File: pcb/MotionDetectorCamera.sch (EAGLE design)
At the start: 79 parts, among them J1 SOLDER-JUMPER, U1 ICE40HX4K-BG121, U2 TPS6280XYKAR, U3 TPS6280XYKAR, U4 W989D6DBGX6I, U5 TPS63805YFFR, U6 GD25LQ80CEIGR, X1 SIT8021AI-J4-18S-12.000000E

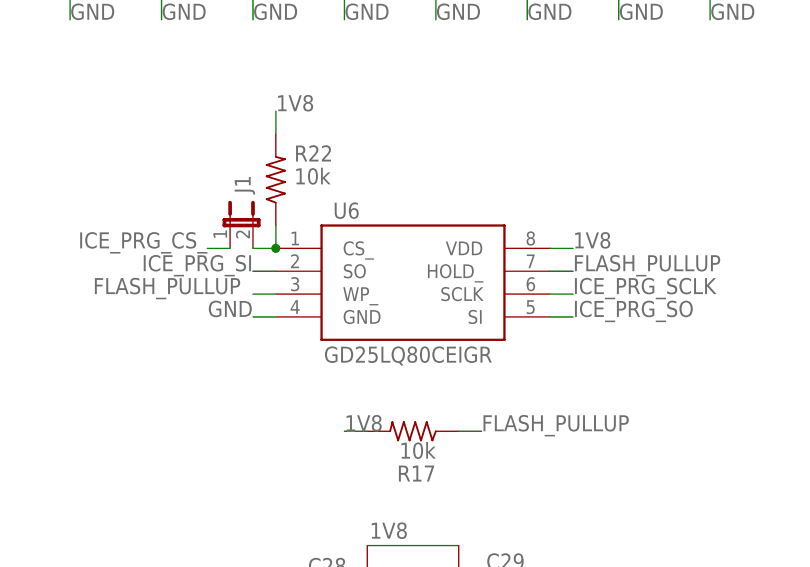
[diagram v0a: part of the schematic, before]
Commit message: Switch to W25Q80EWUXIE
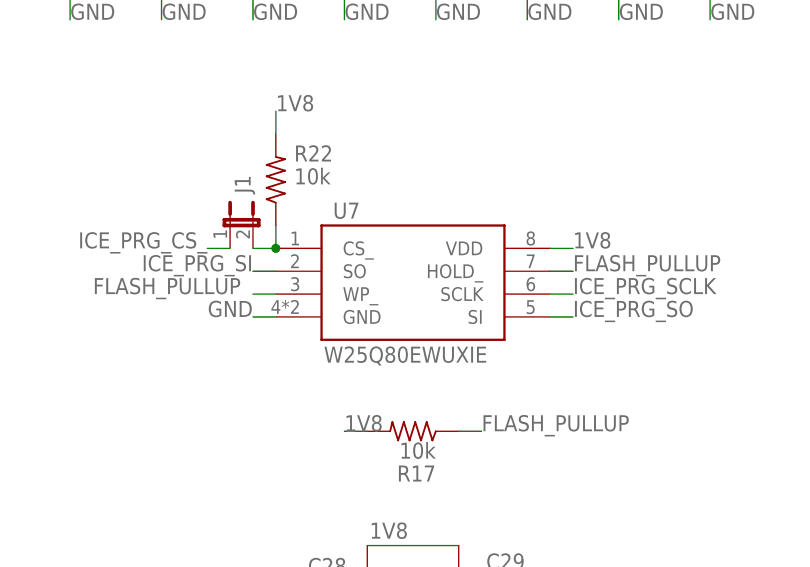
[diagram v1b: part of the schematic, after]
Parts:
- removed U6: GD25LQ80CEIGR, EagleLibrary:GD25LQ80CEIGR
- added U7: W25Q80EWUXIE, EagleLibrary:W25Q80EWUXIE
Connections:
- net 1V8: now also U7.VDD; no longer U6.VDD
- net FLASH_PULLUP: now also U7.HOLD_, U7.WP_; no longer U6.HOLD_, U6.WP_
- net GND: now also U7.GND; no longer U6.GND
- net ICE_PRG_SCLK: now also U7.SCLK; no longer U6.SCLK
- net ICE_PRG_SI: now also U7.SO; no longer U6.SO
- net ICE_PRG_SO: now also U7.SI; no longer U6.SI
- net N$3: now also U7.CS_; no longer U6.CS_
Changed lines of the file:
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@@
 <attribute name="PN" value="GRM155R61H104KE19D"/>
 </part>
-<part name="U6" library="EagleLibrary" deviceset="GD25LQ80CEIGR" device="" package3d_urn="urn:adsk.eagle:package:17077898/1"/>
 <part name="R17" library="EagleLibrary" deviceset="RESISTOR" device="0402" package3d_urn="urn:adsk.eagle:package:17080064/1" value="10k">
 <attribute name="MFG" value="Vishay"/>
@@
 </part>
 <part name="J1" library="EagleLibrary" deviceset="SOLDER-JUMPER" device=""/>
+<part name="U7" library="EagleLibrary" deviceset="W25Q80EWUXIE" device="" package3d_urn="urn:adsk.eagle:package:18792578/1"/>
 </parts>
 <sheets>
@@
 <attribute name="MFG" x="83.82" y="68.58" size="1.778" layer="96" display="off"/>
 </instance>
-<instance part="U6" gate="G$1" x="378.46" y="121.92" smashed="yes">
-<attribute name="NAME" x="369.57" y="127.762" size="1.778" layer="95"/>
-<attribute name="PN" x="368.554" y="111.76" size="1.778" layer="95"/>
-</instance>
 <instance part="R17" gate="G$1" x="378.46" y="104.14" smashed="yes" rot="R180">
 <attribute name="NAME" x="381" y="100.33" size="1.778" layer="95" rot="R180"/>
@@
 <instance part="J1" gate="G$1" x="360.68" y="127" smashed="yes">
 <attribute name="NAME" x="358.648" y="130.556" size="1.778" layer="95" rot="R90" align="top-left"/>
+</instance>
+<instance part="U7" gate="G$1" x="368.3" y="127" smashed="yes">
+<attribute name="NAME" x="369.57" y="127.762" size="1.778" layer="95"/>
+<attribute name="PN" x="368.554" y="111.76" size="1.778" layer="95"/>
 </instance>
 </instances>
@@
 </segment>
 <segment>
-<pinref part="U6" gate="G$1" pin="VDD"/>
 <wire x1="393.7" y1="124.46" x2="396.24" y2="124.46" width="0.1524" layer="91"/>
 <label x="396.24" y="124.46" size="1.778" layer="95"/>
+<pinref part="U7" gate="G$1" pin="VDD"/>
 </segment>
 <segment>
@@
 </segment>
 <segment>
-<pinref part="U6" gate="G$1" pin="GND"/>
 <wire x1="363.22" y1="116.84" x2="360.68" y2="116.84" width="0.1524" layer="91"/>
 <label x="360.68" y="116.84" size="1.778" layer="95" align="bottom-right"/>
+<pinref part="U7" gate="G$1" pin="GND"/>
 </segment>
 <segment>
@@
 </segment>
 <segment>
-<pinref part="U6" gate="G$1" pin="SI"/>
 <wire x1="393.7" y1="116.84" x2="396.24" y2="116.84" width="0.1524" layer="91"/>
 <label x="396.24" y="116.84" size="1.778" layer="95"/>
+<pinref part="U7" gate="G$1" pin="SI"/>
 </segment>
 </net>
@@
 </segment>
 <segment>
-<pinref part="U6" gate="G$1" pin="SO"/>
 <wire x1="363.22" y1="121.92" x2="360.68" y2="121.92" width="0.1524" layer="91"/>
 <label x="360.68" y="121.92" size="1.778" layer="95" align="bottom-right"/>
+<pinref part="U7" gate="G$1" pin="SO"/>
 </segment>
 </net>
@@
 <wire x1="393.7" y1="119.38" x2="396.24" y2="119.38" width="0.1524" layer="91"/>
 <label x="396.24" y="119.38" size="1.778" layer="95"/>
-<pinref part="U6" gate="G$1" pin="SCLK"/>
+<pinref part="U7" gate="G$1" pin="SCLK"/>
 </segment>
 <segment>
@@
 </segment>
 <segment>
-<pinref part="U6" gate="G$1" pin="WP_"/>
 <wire x1="363.22" y1="119.38" x2="360.68" y2="119.38" width="0.1524" layer="91"/>
 <label x="342.9" y="119.38" size="1.778" layer="95"/>
-</segment>
-<segment>
-<pinref part="U6" gate="G$1" pin="HOLD_"/>
+<pinref part="U7" gate="G$1" pin="WP_"/>
+</segment>
+<segment>
 <wire x1="393.7" y1="121.92" x2="396.24" y2="121.92" width="0.1524" layer="91"/>
 <label x="396.24" y="121.92" size="1.778" layer="95"/>
+<pinref part="U7" gate="G$1" pin="HOLD_"/>
 </segment>
 </net>
@@
 <segment>
 <pinref part="J1" gate="G$1" pin="2"/>
-<pinref part="U6" gate="G$1" pin="CS_"/>
 <pinref part="R22" gate="G$1" pin="1"/>
 <wire x1="363.22" y1="124.46" x2="363.22" y2="127" width="0.1524" layer="91"/>
+<wire x1="360.68" y1="124.46" x2="363.22" y2="124.46" width="0.1524" layer="91"/>
+<pinref part="U7" gate="G$1" pin="CS_"/>
 <junction x="363.22" y="124.46"/>
-<wire x1="360.68" y1="124.46" x2="363.22" y2="124.46" width="0.1524" layer="91"/>
-</segment>
-</net>
+</segment>
+</net>

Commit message: Safety commit
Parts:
- removed R9: 10k, EagleLibrary:RESISTOR0402
- C25: value 10u -> 22u; device EagleLibrary:CAPACITOR0603 -> EagleLibrary:CAPACITOR0805; PN GRM188R61A106KE69D -> GRM219R61C226ME15L
- R13: value 365k -> 422k; device EagleLibrary:RESISTOR0603 -> EagleLibrary:RESISTOR0402; PN CR0603-FX-3653ELF -> CR0402-FX-4223GLF
- R14: device EagleLibrary:RESISTOR0603 -> EagleLibrary:RESISTOR0402; PN CR0603-FX-9102ELF -> CR0402-FX-9102GLF
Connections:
- removed net N$2: R9.1, U5.EN
- net VDD: now also U5.EN; no longer R9.2
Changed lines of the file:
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@@
 <attribute name="PN" value="GRM188R61A106KE69D"/>
 </part>
-<part name="C25" library="EagleLibrary" deviceset="CAPACITOR" device="0603" package3d_urn="urn:adsk.eagle:package:17080173/1" value="10u">
+<part name="C25" library="EagleLibrary" deviceset="CAPACITOR" device="0805" package3d_urn="urn:adsk.eagle:package:17080181/1" value="22u">
 <spice>
 <pinmapping spiceprefix="C">
@@
 </spice>
 <attribute name="MFG" value="Murata"/>
-<attribute name="PN" value="GRM188R61A106KE69D"/>
+<attribute name="PN" value="GRM219R61C226ME15L"/>
 </part>
 <part name="C27" library="EagleLibrary" deviceset="CAPACITOR" device="0805" package3d_urn="urn:adsk.eagle:package:17080181/1" value="22u">
@@
 <attribute name="PN4" value="DFE201612E-R47M=P2"/>
 </part>
-<part name="R13" library="EagleLibrary" deviceset="RESISTOR" device="0603" package3d_urn="urn:adsk.eagle:package:17080173/1" value="365k">
+<part name="R13" library="EagleLibrary" deviceset="RESISTOR" device="0402" package3d_urn="urn:adsk.eagle:package:17080064/1" value="422k">
 <attribute name="MFG" value="Bourns"/>
-<attribute name="PN" value="CR0603-FX-3653ELF"/>
-</part>
-<part name="R14" library="EagleLibrary" deviceset="RESISTOR" device="0603" package3d_urn="urn:adsk.eagle:package:17080173/1" value="91k">
+<attribute name="PN" value="CR0402-FX-4223GLF"/>
+</part>
+<part name="R14" library="EagleLibrary" deviceset="RESISTOR" device="0402" package3d_urn="urn:adsk.eagle:package:17080064/1" value="91k">
 <attribute name="MFG" value="Bourns"/>
-<attribute name="PN" value="CR0603-FX-9102ELF"/>
+<attribute name="PN" value="CR0402-FX-9102GLF"/>
 </part>
 <part name="U4" library="EagleLibrary" deviceset="W989D6DBGX6I" device=""/>
@@
 <part name="TP7" library="EagleLibrary" deviceset="UFL-CONNECTOR" device=""/>
 <part name="TP6" library="EagleLibrary" deviceset="UFL-CONNECTOR" device=""/>
-<part name="R9" library="EagleLibrary" deviceset="RESISTOR" device="0402" package3d_urn="urn:adsk.eagle:package:17080064/1" value="10k">
-<attribute name="MFG" value="Vishay"/>
-<attribute name="PN" value="CRCW040210K0FKEDC"/>
-</part>
 <part name="R1" library="EagleLibrary" deviceset="RESISTOR" device="1206" package3d_urn="urn:adsk.eagle:package:17080198/1" value="1">
 <attribute name="MFG" value="Vishay"/>
@@
 <attribute name="NAME" x="315.722" y="50.8" size="1.778" layer="95" rot="R270"/>
 </instance>
-<instance part="R9" gate="G$1" x="317.5" y="274.32" smashed="yes" rot="R90">
-<attribute name="NAME" x="313.69" y="271.78" size="1.778" layer="95" rot="R90"/>
-<attribute name="VALUE" x="316.23" y="271.78" size="1.778" layer="96" rot="R90"/>
-<attribute name="MFG" x="317.5" y="274.32" size="1.778" layer="96" rot="R90" display="off"/>
-<attribute name="PN" x="317.5" y="274.32" size="1.778" layer="96" rot="R90" display="off"/>
-</instance>
 <instance part="R1" gate="G$1" x="43.18" y="254" smashed="yes" rot="R180">
 <attribute name="NAME" x="45.72" y="250.19" size="1.778" layer="95" rot="R180"/>
@@
 <wire x1="312.42" y1="264.16" x2="312.42" y2="266.7" width="0.1524" layer="91"/>
 <pinref part="C25" gate="G$1" pin="1"/>
-</segment>
-<segment>
-<pinref part="R9" gate="G$1" pin="2"/>
-<wire x1="317.5" y1="279.4" x2="317.5" y2="281.94" width="0.1524" layer="91"/>
-<label x="317.5" y="281.94" size="1.778" layer="95"/>
+<pinref part="U5" gate="G$1" pin="EN"/>
+<wire x1="320.04" y1="266.7" x2="320.04" y2="259.08" width="0.1524" layer="91"/>
+<junction x="320.04" y="266.7"/>
 </segment>
 <segment>
@@
 </segment>
 </net>
-<net name="N$2" class="0">
-<segment>
-<pinref part="U5" gate="G$1" pin="EN"/>
-<wire x1="320.04" y1="259.08" x2="317.5" y2="259.08" width="0.1524" layer="91"/>
-<wire x1="317.5" y1="259.08" x2="317.5" y2="269.24" width="0.1524" layer="91"/>
-<pinref part="R9" gate="G$1" pin="1"/>
-</segment>
-</net>

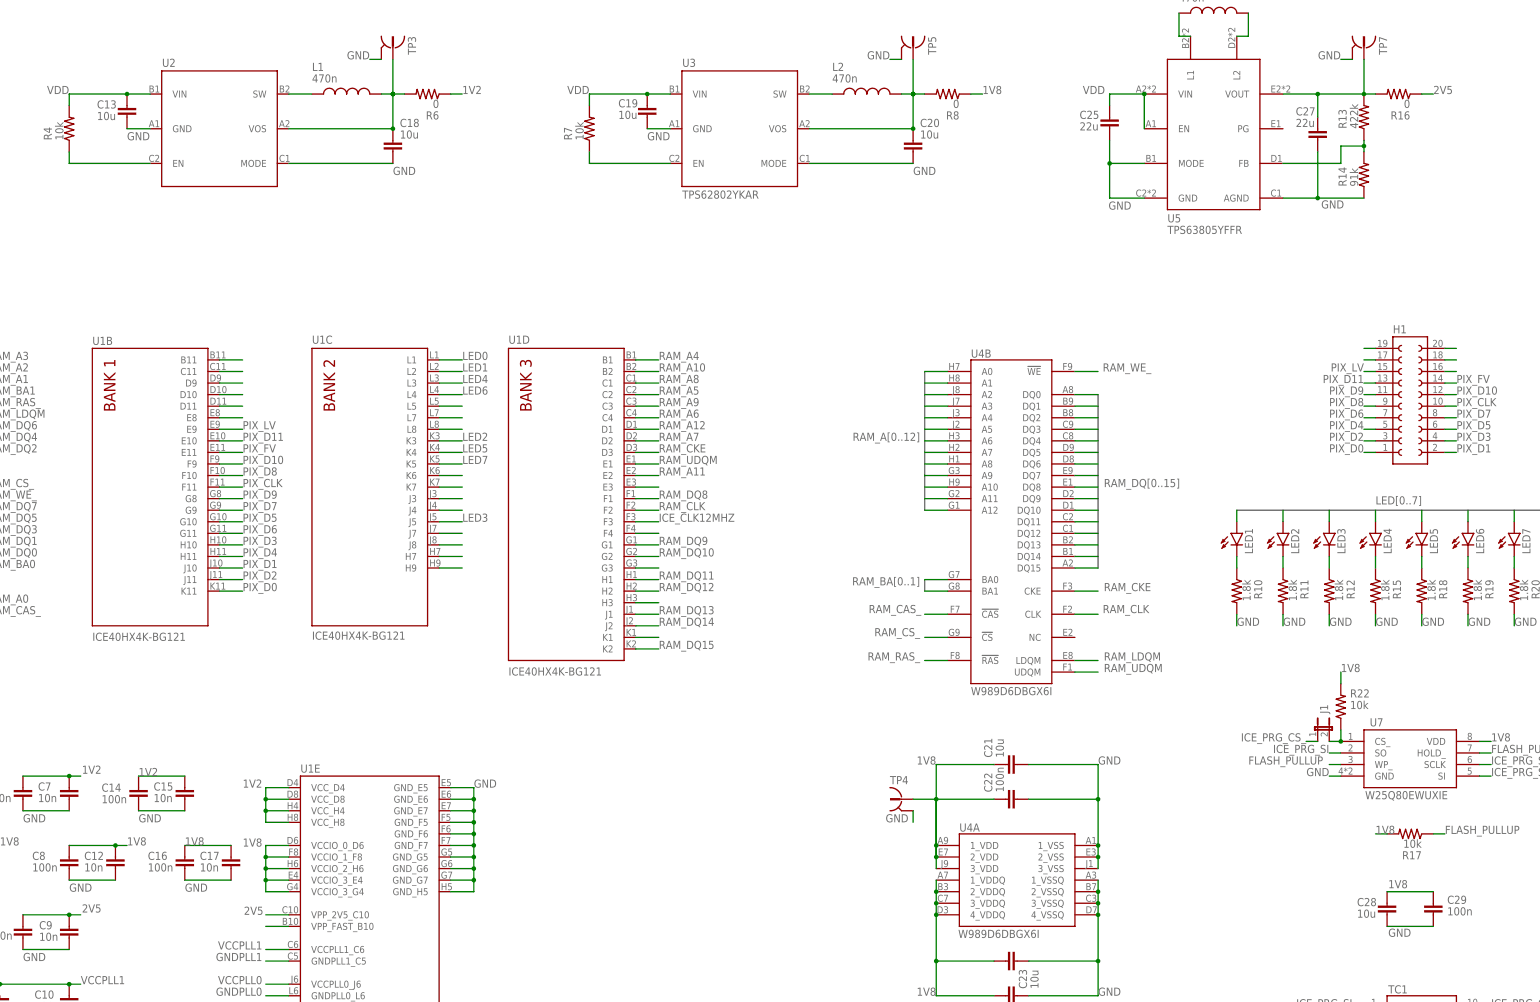
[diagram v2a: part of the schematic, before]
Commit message: Rename 2V5 -> 2V8
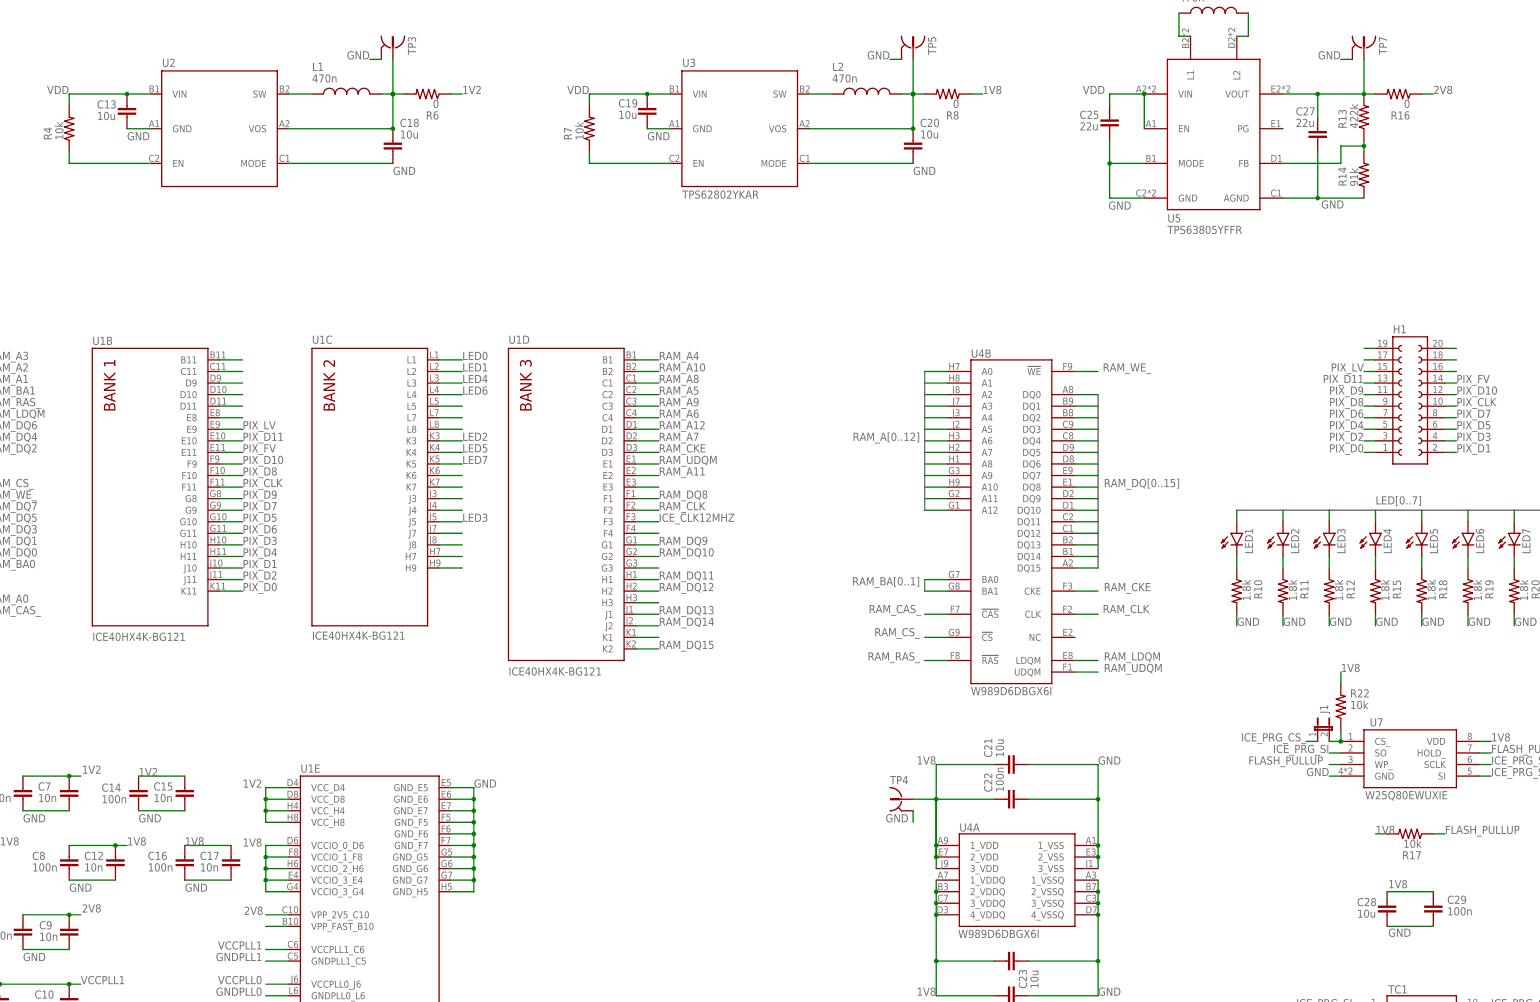
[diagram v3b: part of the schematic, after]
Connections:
- net 2V5 renamed 2V8
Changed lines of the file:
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@@
 </segment>
 </net>
-<net name="2V5" class="0">
+<net name="2V8" class="0">
 <segment>
 <pinref part="R16" gate="G$1" pin="1"/>

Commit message: Laying out AR0330
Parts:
- added C30, C32, C34, C36, C38: 100n, EagleLibrary:CAPACITOR0402
- added C31, C33, C35, C37, C39: 10n, EagleLibrary:CAPACITOR0402
- added U6: AR0330CS1C12SPKA0, EagleLibrary:AR0330CS1C12SPKA0
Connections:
- removed net ICE_CLK12MHZ: TP6.SIGNAL, U1D.F3, X1.OUT
- new net CLK12MHZ: TP6.SIGNAL, U1D.F3, U6G$2.EXTCLK, X1.OUT
- new net GND10: C36.2, C37.2
- new net GND11: C38.2, C39.2
- new net GND7: C30.2, C31.2
- new net GND8: C32.2, C33.2
- new net GND9: C34.2, C35.2
- new net PIX_RST_: U6G$2.RST_
- new net PIX_SCLK: U6G$2.SCLK
- new net PIX_SDATA: U6G$2.SDATA
- net 1V8: now also C34.1, C35.1, C36.1, C37.1, U6G$1.VDD, U6G$1.VDD_IO
- net 2V8: now also C30.1, C31.1, C32.1, C33.1, C38.1, C39.1, U6G$1.VAA, U6G$1.VAA_PIX, U6G$1.VDD_MIPI, U6G$1.VDD_PLL
- net GND: now also U6G$1.AGND, U6G$1.DGND, U6G$2.SADDR, U6G$2.TEST
- net PIX_CLK: now also U6G$2.PIXCLK
- net PIX_D0: now also U6G$2.DOUT0
- net PIX_D1: now also U6G$2.DOUT1
- net PIX_D10: now also U6G$2.DOUT10
- net PIX_D11: now also U6G$2.DOUT11
- net PIX_D2: now also U6G$2.DOUT2
- net PIX_D3: now also U6G$2.DOUT3
- net PIX_D4: now also U6G$2.DOUT4
- net PIX_D5: now also U6G$2.DOUT5
- net PIX_D6: now also U6G$2.DOUT6
- net PIX_D7: now also U6G$2.DOUT7
- net PIX_D8: now also U6G$2.DOUT8
- net PIX_D9: now also U6G$2.DOUT9
- net PIX_FV: now also U6G$2.FRAME_VALID
- net PIX_LV: now also U6G$2.LINE_VALID
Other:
- moved on the sheet: C28, C29, H1, J1, R17, R22, U7

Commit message: More progress laying out AR0300
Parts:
- removed H1: HEADER, EagleLibrary:HEADER
- added R9: 10k, EagleLibrary:RESISTOR0402
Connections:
- net RAM_LDQM renamed RAM_DQM0
- net RAM_UDQM renamed RAM_DQM1
- removed net N$36: H1.16
- removed net N$37: H1.17
- removed net N$38: H1.18
- removed net N$39: H1.19
- removed net N$40: H1.20
- removed net N$90: U1B.D10
- removed net N$91: U1B.D11
- removed net N$92: U1B.E8
- net 1V8: now also R9.2
- net PIX_CLK: no longer H1.10
- net PIX_D0: no longer H1.1
- net PIX_D1: no longer H1.2
- net PIX_D10: no longer H1.12
- net PIX_D11: no longer H1.13
- net PIX_D2: no longer H1.3
- net PIX_D3: now also U1B.H11; no longer H1.4, U1B.H10
- net PIX_D4: now also U1B.G11; no longer H1.5, U1B.H11
- net PIX_D5: now also U1B.H10; no longer H1.6, U1B.G10
- net PIX_D6: now also U1B.G9; no longer H1.7, U1B.G11
- net PIX_D7: now also U1B.F10; no longer H1.8, U1B.G9
- net PIX_D8: now also U1B.G10; no longer H1.9, U1B.F10
- net PIX_D9: no longer H1.11
- net PIX_FV: now also U1B.D11; no longer H1.14, U1B.E11
- net PIX_LV: no longer H1.15
- net PIX_RST_: now also R9.1, U1B.E8
- net PIX_SCLK: now also U1B.E11
- net PIX_SDATA: now also U1B.D10

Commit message: Add decoupling capacitors to image sensor
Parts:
- added C40: 10u, EagleLibrary:CAPACITOR0603
- added C41: 100n, EagleLibrary:CAPACITOR0402
- C30, C32, C34, C36, C38: value 100n -> 10u; device EagleLibrary:CAPACITOR0402 -> EagleLibrary:CAPACITOR0603; PN GRM155R61H104KE19D -> GRM188R61A106KE69D
- C31, C33, C35, C37, C39: value 10n -> 100n; PN GCM155R71H103JA55D -> GRM155R61H104KE19D
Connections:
- removed net GND10: C36.2, C37.2
- removed net GND11: C38.2, C39.2
- removed net GND7: C30.2, C31.2
- removed net GND8: C32.2, C33.2
- removed net GND9: C34.2, C35.2
- removed net N$88: U1B.C11
- new net N$1: U1D.F3
- net 1V8: now also C40.1, C41.1
- net CLK12MHZ: now also U1B.C11; no longer U1D.F3
- net GND: now also C30.2, C31.2, C32.2, C33.2, C34.2, C35.2, C36.2, C37.2, C38.2, C39.2, C40.2, C41.2, X1.EN_; no longer X1.ST
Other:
- note added: "VAA Bypassing"
- note added: "VAA_PIX Bypassing"
- note added: "VDD Bypassing"
- note added: "VDD_IO Bypassing"
- note added: "VDD_PLL Bypassing"
- moved on the sheet: C26, C30, C31, C32, C33, C34, C35, C36, C37, C38, C39, R9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
